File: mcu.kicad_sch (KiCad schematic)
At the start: 27 parts, among them U3 STM32F405RGTx, Y1 8 MHz

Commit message: WIP filters
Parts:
- C10, C11, C12, C15, C16, C2, C22, C3, C4, C6, C9: symbol Device:C -> Device:C_Small
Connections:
- net I2C_SCL: now reaches U3.58 (PB6)
- net I2C_SDA: now reaches U3.59 (PB7)
- net AUDIO_IN renamed AUDIO_IN_FILT
- net BASEBAND_IN renamed BASEBAND_IN_FILT
- no-connect marks 31 -> 29
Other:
- moved on the sheet: C10, C11, C12, C15, C16, C2, C22, C3, C4, C6, C9

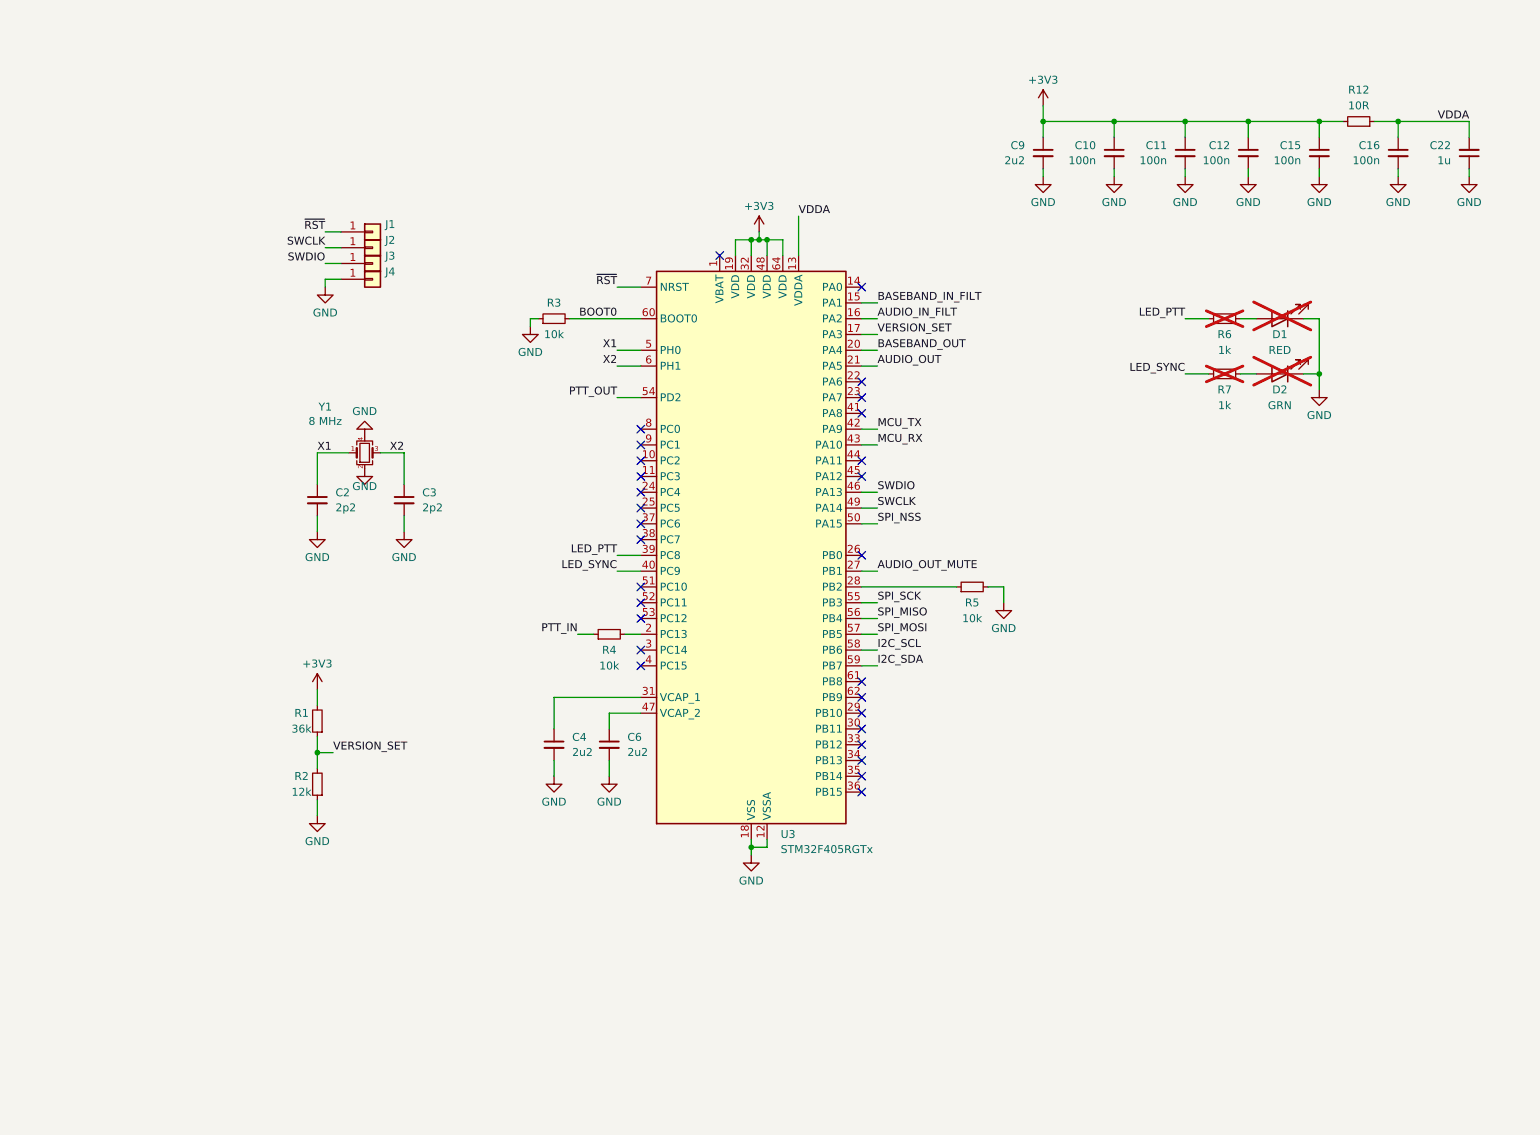
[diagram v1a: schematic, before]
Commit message: First Edits
Added J1 connector, finished filters and swapped µC to STM32G473
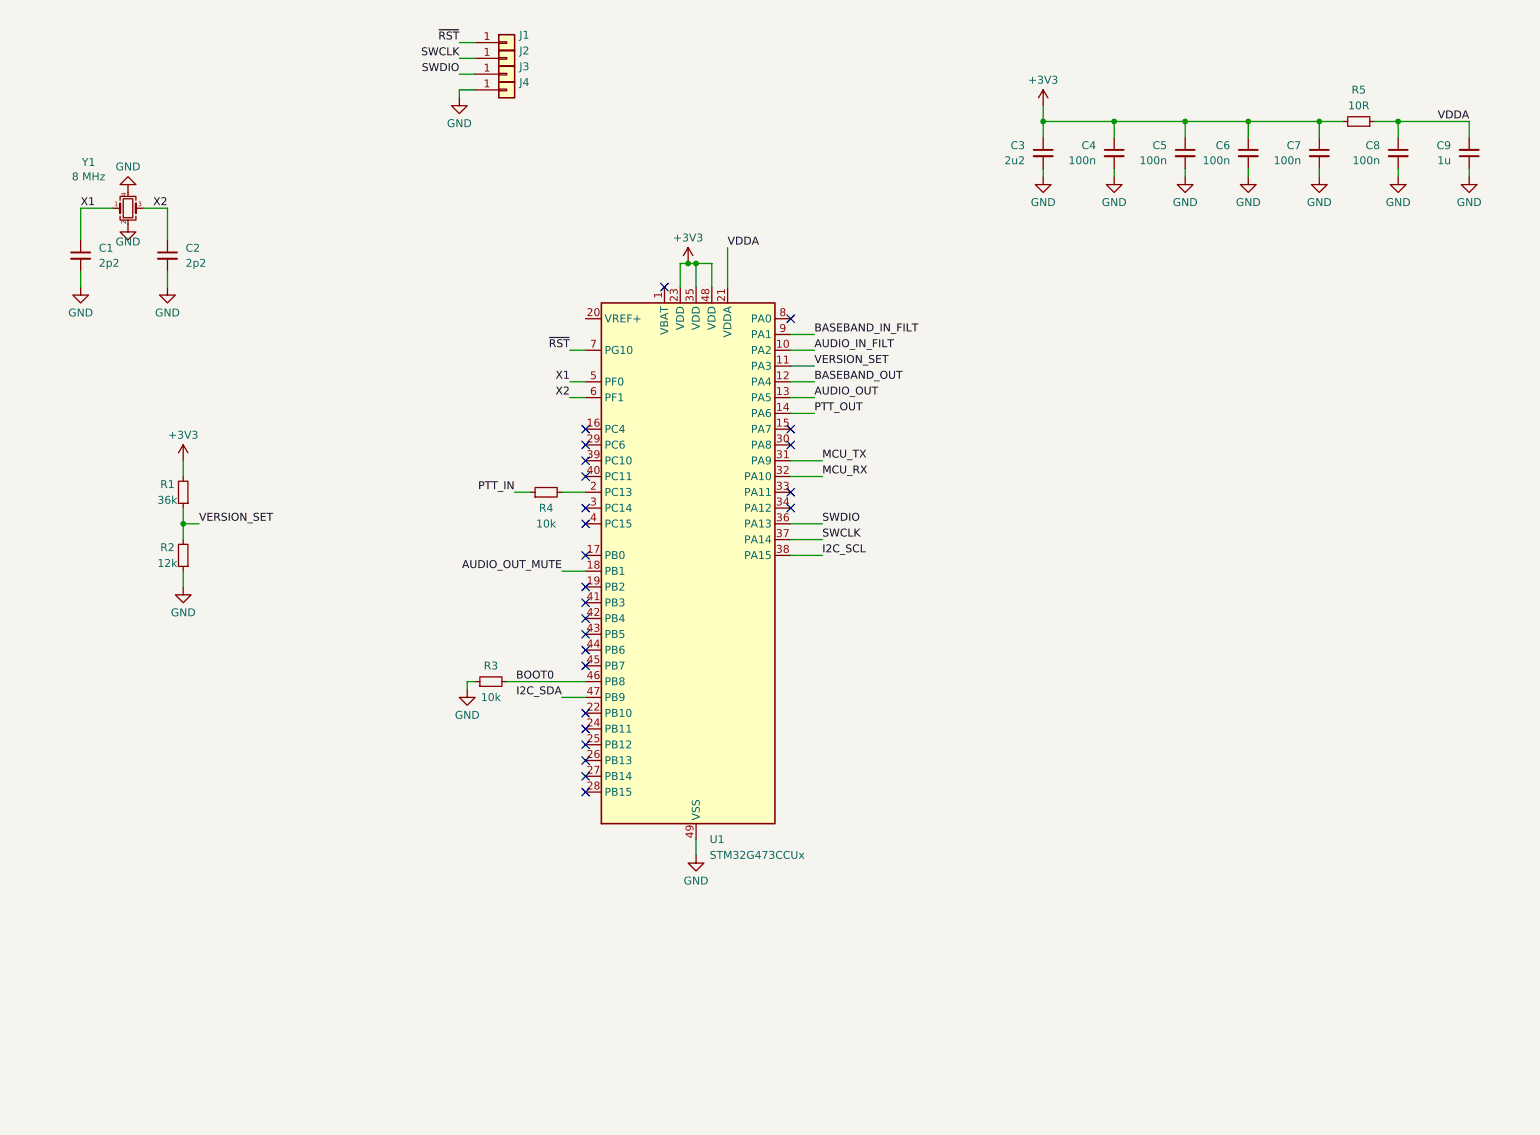
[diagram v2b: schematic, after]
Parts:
- removed C4, C6: 2u2, Capacitor_SMD:C_0603_1608Metric, symbol Device:C_Small
- removed D1: RED, symbol Device:LED
- removed D2: GRN, symbol Device:LED
- removed R5: 10k, Resistor_SMD:R_0603_1608Metric, symbol Device:R_Small
- removed R6, R7: 1k, Resistor_SMD:R_0603_1608Metric, symbol Device:R_Small
- removed U3: STM32F405RGTx, Package_QFP:LQFP-64_10x10mm_P0.5mm, symbol MCU_ST_STM32F4:STM32F405RGTx
- added U1: STM32G473CCUx, Package_DFN_QFN:QFN-48-1EP_7x7mm_P0.5mm_EP5.6x5.6mm, symbol MCU_ST_STM32G4:STM32G473CCUx
- C1: renamed from C2; footprint Capacitor_SMD:C_0603_1608Metric -> Capacitor_SMD:C_0201_0603Metric
- C2: renamed from C3; footprint Capacitor_SMD:C_0603_1608Metric -> Capacitor_SMD:C_0201_0603Metric
- C3: renamed from C9; footprint Capacitor_SMD:C_0603_1608Metric -> Capacitor_SMD:C_0201_0603Metric
- C4: renamed from C10; footprint Capacitor_SMD:C_0603_1608Metric -> Capacitor_SMD:C_0201_0603Metric
- C5: renamed from C11; footprint Capacitor_SMD:C_0603_1608Metric -> Capacitor_SMD:C_0201_0603Metric
- C6: renamed from C12; footprint Capacitor_SMD:C_0603_1608Metric -> Capacitor_SMD:C_0201_0603Metric
- C7: renamed from C15; footprint Capacitor_SMD:C_0603_1608Metric -> Capacitor_SMD:C_0201_0603Metric
- C8: renamed from C16; footprint Capacitor_SMD:C_0603_1608Metric -> Capacitor_SMD:C_0201_0603Metric
- C9: renamed from C22; footprint Capacitor_SMD:C_0603_1608Metric -> Capacitor_SMD:C_0201_0603Metric
- R1, R2, R3, R4: footprint Resistor_SMD:R_0603_1608Metric -> Resistor_SMD:R_0201_0603Metric
- R5: renamed from R12; footprint Resistor_SMD:R_0603_1608Metric -> Resistor_SMD:R_0201_0603Metric
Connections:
- net +3V3: now also U1.23 (VDD), U1.35 (VDD), U1.48 (VDD)
- net AUDIO_IN_FILT: now also U1.10 (PA2)
- net AUDIO_OUT: now also U1.13 (PA5)
- net AUDIO_OUT_MUTE: now also U1.18 (PB1)
- net BASEBAND_IN_FILT: now also U1.9 (PA1)
- net BASEBAND_OUT: now also U1.12 (PA4)
- net BOOT0: now also U1.46 (PB8)
- net GND: now also U1.49 (VSS)
- net I2C_SCL: now also U1.38 (PA15)
- net I2C_SDA: now also U1.47 (PB9)
- net MCU_RX: now also U1.32 (PA10)
- net MCU_TX: now also U1.31 (PA9)
- net PTT_OUT: now also U1.14 (PA6)
- net SWCLK: now also U1.37 (PA14)
- net SWDIO: now also U1.36 (PA13)
- net VDDA: now also U1.21 (VDDA)
- net VERSION_SET: now also U1.11 (PA3)
- net X1: now also U1.5 (PF0)
- net X2: now also U1.6 (PF1)
- net ~{RST}: now also U1.7 (PG10)
- net at R4.2: now also U1.2 (PC13)
- no-connect marks 29 -> 25
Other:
- moved on the sheet: C1, C2, J1, J2, J3, J4, R1, R2, R3, Y1

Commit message: PCB routed, gerbers and ibom included
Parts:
- removed J1, J2, J3, J4: ~, TestPoint:TestPoint_Pad_D1.5mm, symbol Connector_Generic:Conn_01x01
- added J1: Conn_01x04, Connector_Harwin:Harwin_M20-89004xx_1x04_P2.54mm_Horizontal, symbol Connector_Generic:Conn_01x04
- added SYM1: SYM_ESD_Small, Symbol:ESD-Logo_6.6x6mm_SilkScreen, symbol Graphic:SYM_ESD_Small
- added SYM2: Logo_Open_Hardware_Small, Symbol:OSHW-Logo_5.7x6mm_SilkScreen, symbol Graphic:Logo_Open_Hardware_Small
- C1, C2, C3, C4, C5, C6, C7, C8, C9: footprint Capacitor_SMD:C_0201_0603Metric -> Capacitor_SMD:C_0402_1005Metric
- R1, R2, R3, R4, R5: footprint Resistor_SMD:R_0201_0603Metric -> Resistor_SMD:R_0402_1005Metric
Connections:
- net GND: now also J1.4 (Pin_4)
- net SWCLK: now also J1.2 (Pin_2)
- net SWDIO: now also J1.3 (Pin_3)
- net ~{RST}: now also J1.1 (Pin_1)
